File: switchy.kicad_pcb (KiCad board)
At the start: 2 copper layers, 20.2 x 16.2 mm, 4 parts, among them J1 LED CONNECT, J2 BOARD CONNECTIONS

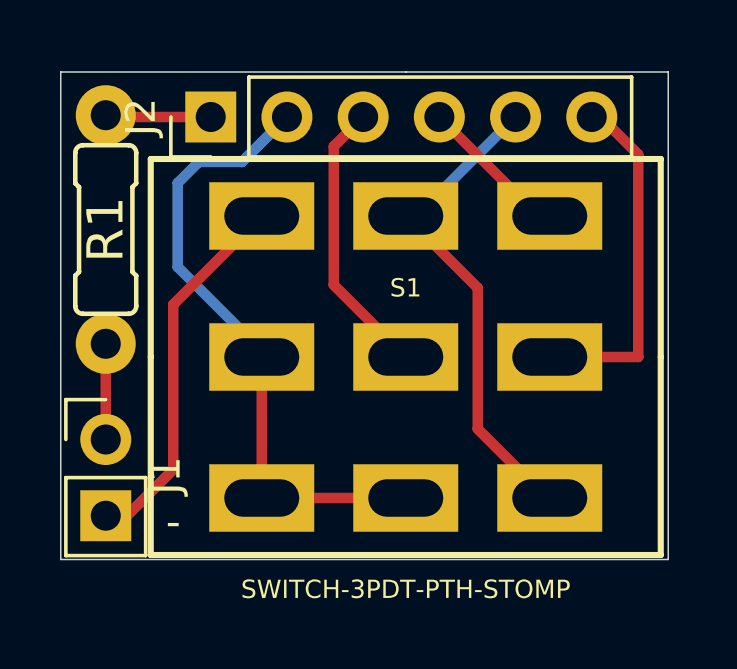
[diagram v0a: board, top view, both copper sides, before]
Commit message: update with kicad 7, improved silkscreen labels
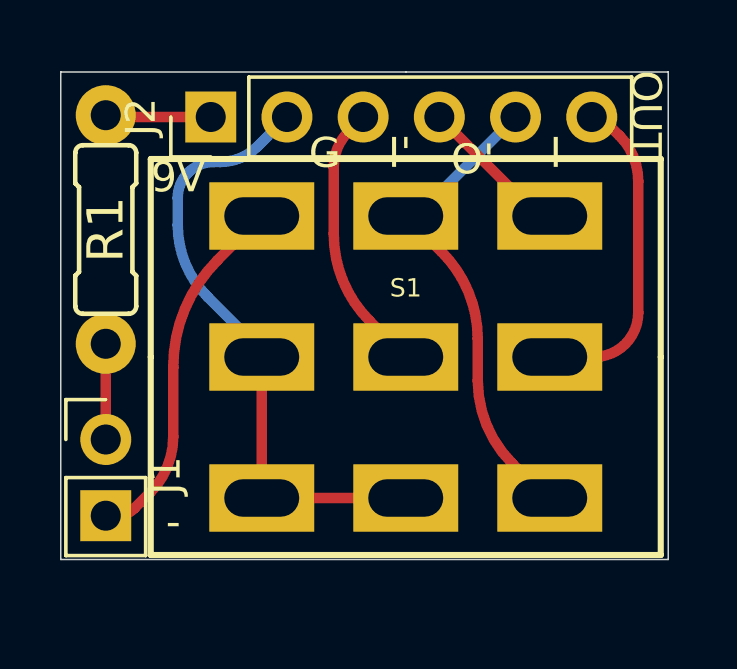
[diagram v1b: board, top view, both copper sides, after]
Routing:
- net OUTPUT: track 11.8 -> 11.0 mm
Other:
- net class Default removed
- board text added: "9V"
- board text added: "CLR"
- board text added: "G"
- board text added: "I'"
- board text added: "O'"
- board text added: "OUT"
- board text removed: "B"
- board text removed: "E"
- board text removed: "O"
